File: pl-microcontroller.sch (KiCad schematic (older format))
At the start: 104 parts, among them J13 Prog, J14 Button, J15 Charger, J16 Seven-segment, J17 LOAD, Q21 MMBT2222A, Q22 MMBT2222A, Q23 MMBT2222A, Q24 MMBT2222A, Q25 MMBT2222A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

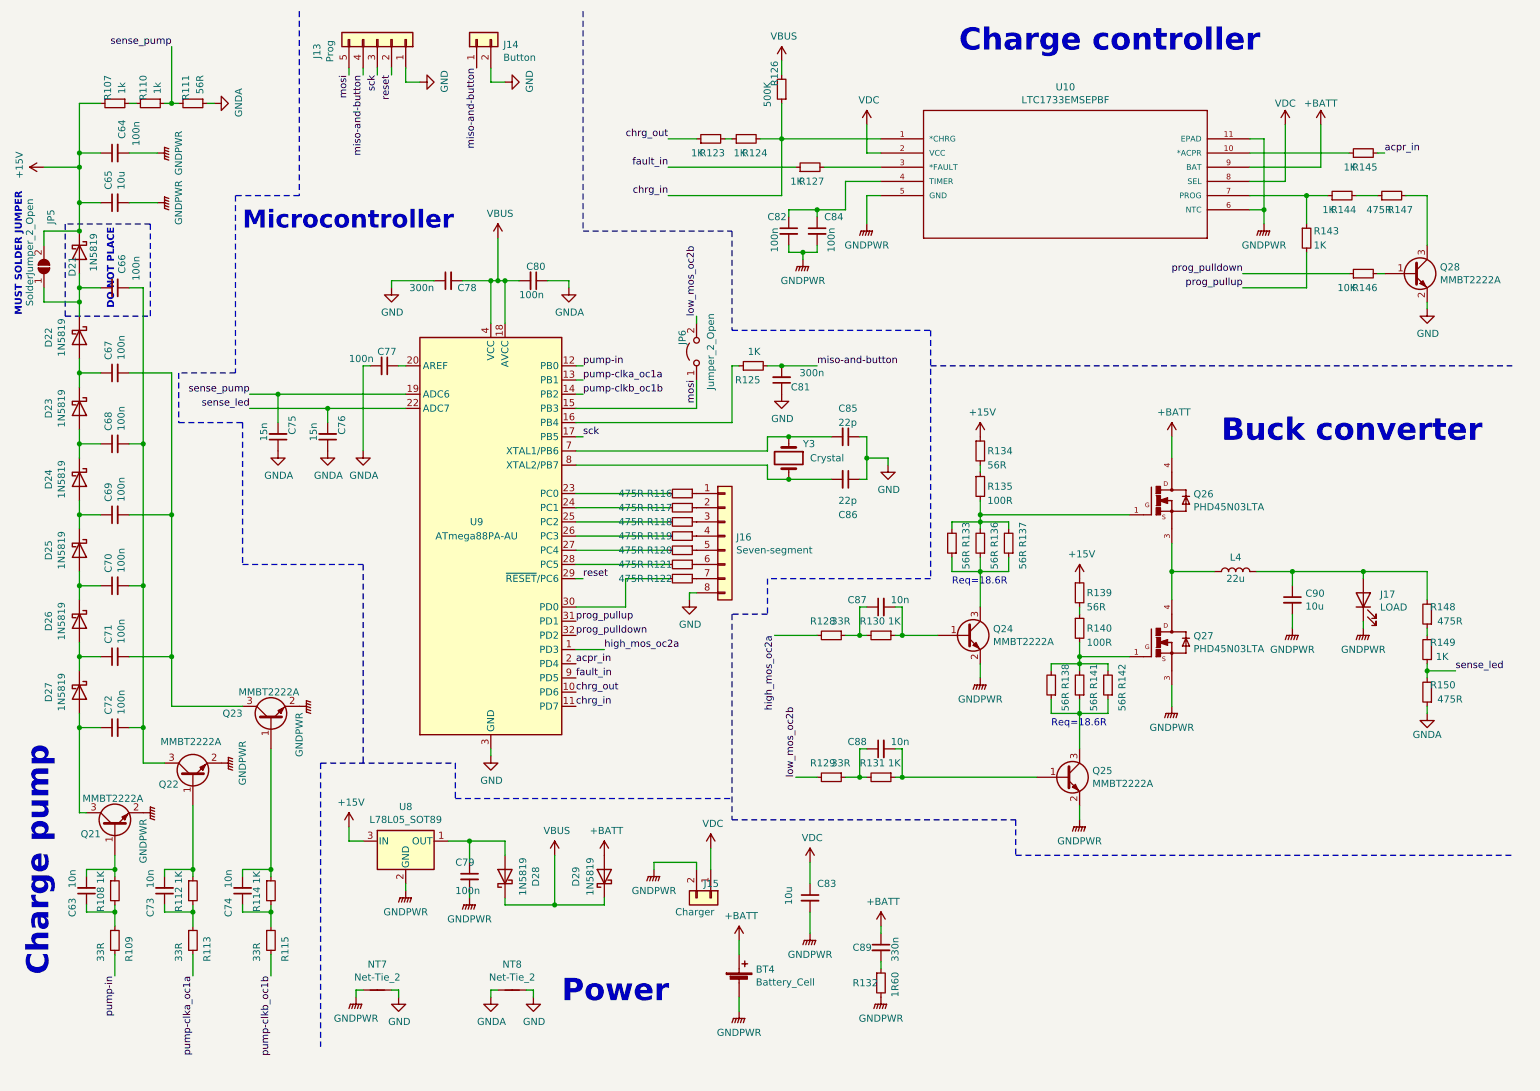
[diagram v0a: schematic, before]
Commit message: Fixed hierarchical sheet for microcontroller unit
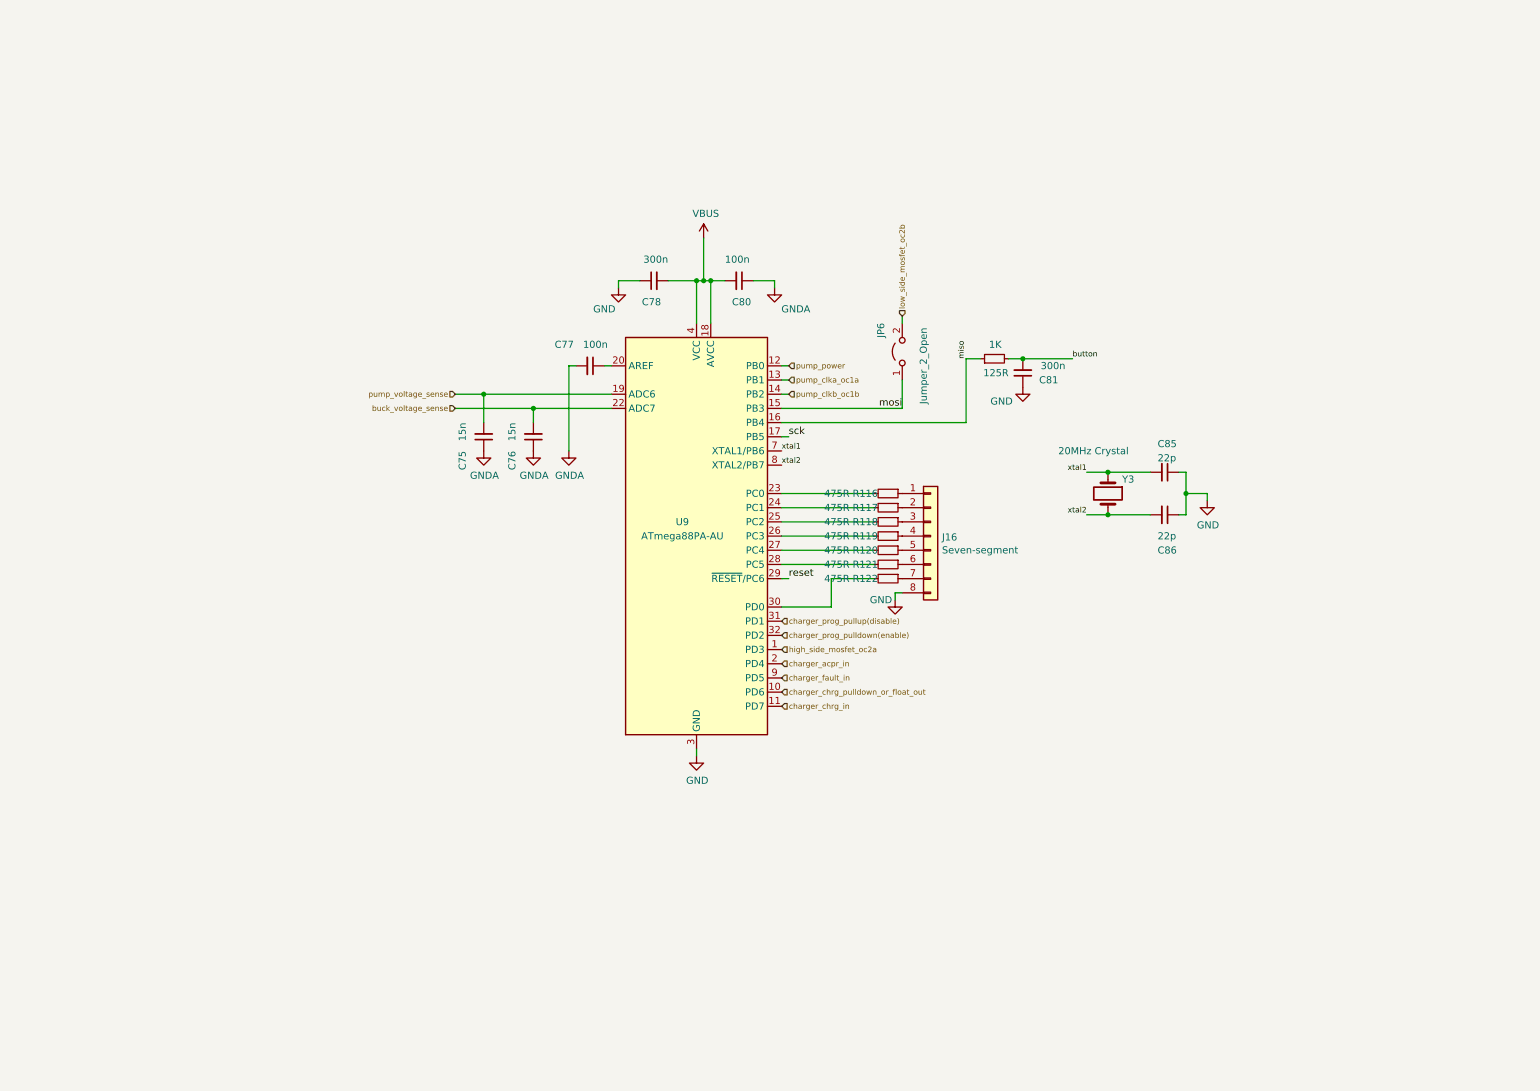
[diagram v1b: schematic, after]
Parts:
- removed BT4: Battery_Cell, Connector_PinHeader_2.54mm:PinHeader_1x02_P2.54mm_Vertical, symbol portable-light-rescue:Battery_Cell-Device
- removed C63, C73, C74, C87, C88: 10n, Capacitor_SMD:C_1206_3216Metric_Pad1.42x1.75mm_HandSolder, symbol portable-light-rescue:C_Small-Device
- removed C64, C66, C67, C68, C69, C70, C71, C72, C79, C82, C84: 100n, Capacitor_SMD:C_1206_3216Metric_Pad1.42x1.75mm_HandSolder, symbol portable-light-rescue:C_Small-Device
- removed C65, C83, C90: 10u, Capacitor_THT:C_Radial_D5.0mm_H7.0mm_P2.00mm, symbol portable-light-rescue:C_Small-Device
- removed C89: 330n, Capacitor_SMD:C_1206_3216Metric_Pad1.42x1.75mm_HandSolder, symbol portable-light-rescue:C_Small-Device
- removed D21, D22, D23, D24, D25, D26, D27: 1N5819, Diode_SMD:D_SMA_Handsoldering, symbol portable-light-rescue:1N5819-Diode
- removed D28, D29: 1N5819, Diode_THT:D_DO-41_SOD81_P12.70mm_Horizontal, symbol portable-light-rescue:1N5819-Diode
- removed J13: Prog, Connector_PinHeader_2.54mm:PinHeader_1x05_P2.54mm_Vertical, symbol portable-light-rescue:Conn_01x05-Connector_Generic
- removed J14: Button, Ribbon_Cable:Ribbon_2, symbol portable-light-rescue:Conn_01x02-Connector_Generic
- removed J15: Charger, Connector_PinHeader_2.54mm:PinHeader_1x02_P2.54mm_Vertical, symbol portable-light-rescue:Conn_01x02-Connector_Generic
- removed J17: LOAD, Connector_PinHeader_2.54mm:PinHeader_1x02_P2.54mm_Vertical, symbol portable-light-rescue:LED-Device
- removed JP5: SolderJumper_2_Open, Jumper:SolderJumper-2_P1.3mm_Open_TrianglePad1.0x1.5mm, symbol portable-light-rescue:SolderJumper_2_Open-Jumper
- removed L4: 22u, Capacitor_THT:CP_Radial_D8.0mm_P5.00mm, symbol portable-light-rescue:L-Device
- removed NT7, NT8: Net-Tie_2, NetTie:NetTie-2_SMD_Pad0.5mm, symbol portable-light-rescue:Net-Tie_2-Device
- removed Q21, Q22, Q23, Q24, Q25, Q28: MMBT2222A, Package_TO_SOT_SMD:SOT-23, symbol portable-light-rescue:MMBT3904-Transistor_BJT
- removed Q26, Q27: PHD45N03LTA, UniX_Generic:DPAK, symbol portable-light-rescue:PHD45N03LTA-PHD45N03LTA
- removed R107, R110: 1k, Resistor_SMD:R_0603_1608Metric_Pad1.05x0.95mm_HandSolder, symbol portable-light-rescue:R_Small-Device
- removed R108, R112, R114, R123, R124, R127, R130, R131, R143, R144, R145, R149: 1K, Resistor_SMD:R_0603_1608Metric_Pad1.05x0.95mm_HandSolder, symbol portable-light-rescue:R_Small-Device
- removed R109, R113, R115, R128, R129: 33R, Resistor_SMD:R_0805_2012Metric_Pad1.15x1.40mm_HandSolder, symbol portable-light-rescue:R_Small-Device
- removed R111, R133, R134, R136, R137, R138, R139, R141, R142: 56R, Resistor_SMD:R_0805_2012Metric_Pad1.15x1.40mm_HandSolder, symbol portable-light-rescue:R_Small-Device
- removed R126: 500K, Resistor_THT:R_Axial_DIN0309_L9.0mm_D3.2mm_P12.70mm_Horizontal, symbol portable-light-rescue:R_Small-Device
- removed R132: 1R60, Resistor_SMD:R_0805_2012Metric_Pad1.15x1.40mm_HandSolder, symbol portable-light-rescue:R_Small-Device
- removed R135, R140: 100R, Resistor_SMD:R_1206_3216Metric_Pad1.42x1.75mm_HandSolder, symbol portable-light-rescue:R_Small-Device
- removed R146: 10K, Resistor_SMD:R_1206_3216Metric_Pad1.42x1.75mm_HandSolder, symbol portable-light-rescue:R_Small-Device
- removed R147, R148: 475R, Resistor_SMD:R_1206_3216Metric_Pad1.42x1.75mm_HandSolder, symbol portable-light-rescue:R_Small-Device
- removed R150: 475R, Resistor_SMD:R_0805_2012Metric_Pad1.15x1.40mm_HandSolder, symbol portable-light-rescue:R_Small-Device
- removed U10: LTC1733EMSEPBF, UniX_Generic:MSOP-10_MSE, symbol portable-light-rescue:LTC1733EMSEPBF-LTC1733
- removed U8: L78L05_SOT89, Package_TO_SOT_SMD:SOT-89-3, symbol portable-light-rescue:L78L05_SOT89-Regulator_Linear
- Y3: value Crystal -> 20MHz Crystal
- renumbered R125 to 125R
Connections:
- net xtal1: now reaches C85.2, U9.7 (XTAL1/PB6), Y3.1
- net xtal2: now reaches C86.2, U9.8 (XTAL2/PB7), Y3.2
- net miso: now reaches 125R.1, U9.16 (PB4)
- net acpr_in renamed charger_acpr_in
- net chrg_in renamed charger_chrg_in
- net chrg_out renamed charger_chrg_pulldown_or_float_out
- net fault_in renamed charger_fault_in
- net high_mos_oc2a renamed high_side_mosfet_oc2a
- net low_mos_oc2b renamed low_side_mosfet_oc2b
- net miso-and-button renamed button
- net prog_pulldown renamed charger_prog_pulldown(enable)
- net prog_pullup renamed charger_prog_pullup(disable)
- net pump-clka_oc1a renamed pump_clka_oc1a
- net pump-clkb_oc1b renamed pump_clkb_oc1b
- net pump-in renamed pump_power
- net sense_led renamed buck_voltage_sense
- net sense_pump renamed pump_voltage_sense
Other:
- note removed: "Buck converter"
- note removed: "Charge controller"
- note removed: "Charge pump"
- note removed: "DO NOT PLACE"
- note removed: "MUST SOLDER JUMPER"
- note removed: "Microcontroller"
- note removed: "Power"
- note removed: "Req=18.6R"
- moved on the sheet: 125R, C75, C76, C77, C78, C80, C81, C85, C86, J16, JP6, R116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
